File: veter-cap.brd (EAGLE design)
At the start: 101.6 x 78.7 mm, 36 parts, among them IC1 7805TV

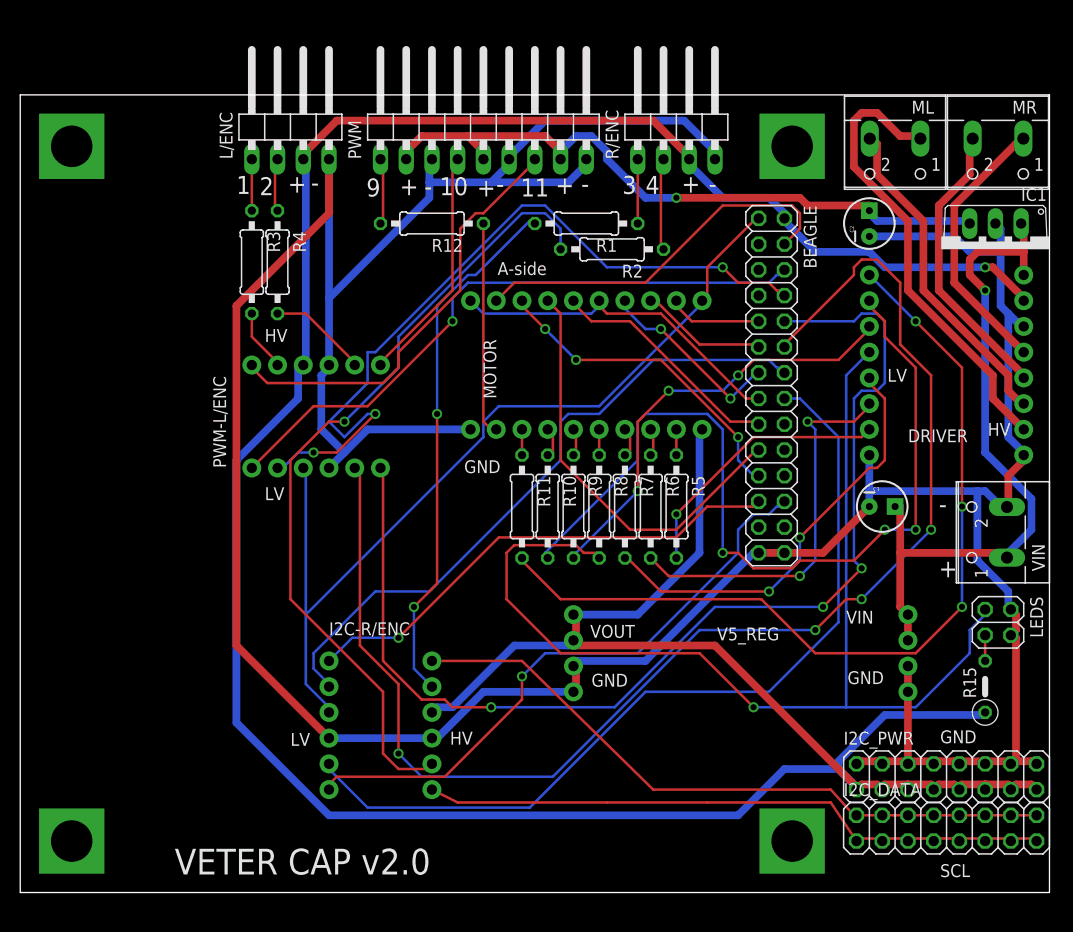
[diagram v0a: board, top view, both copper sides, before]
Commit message: version 3.0 of the cap, fixed connector
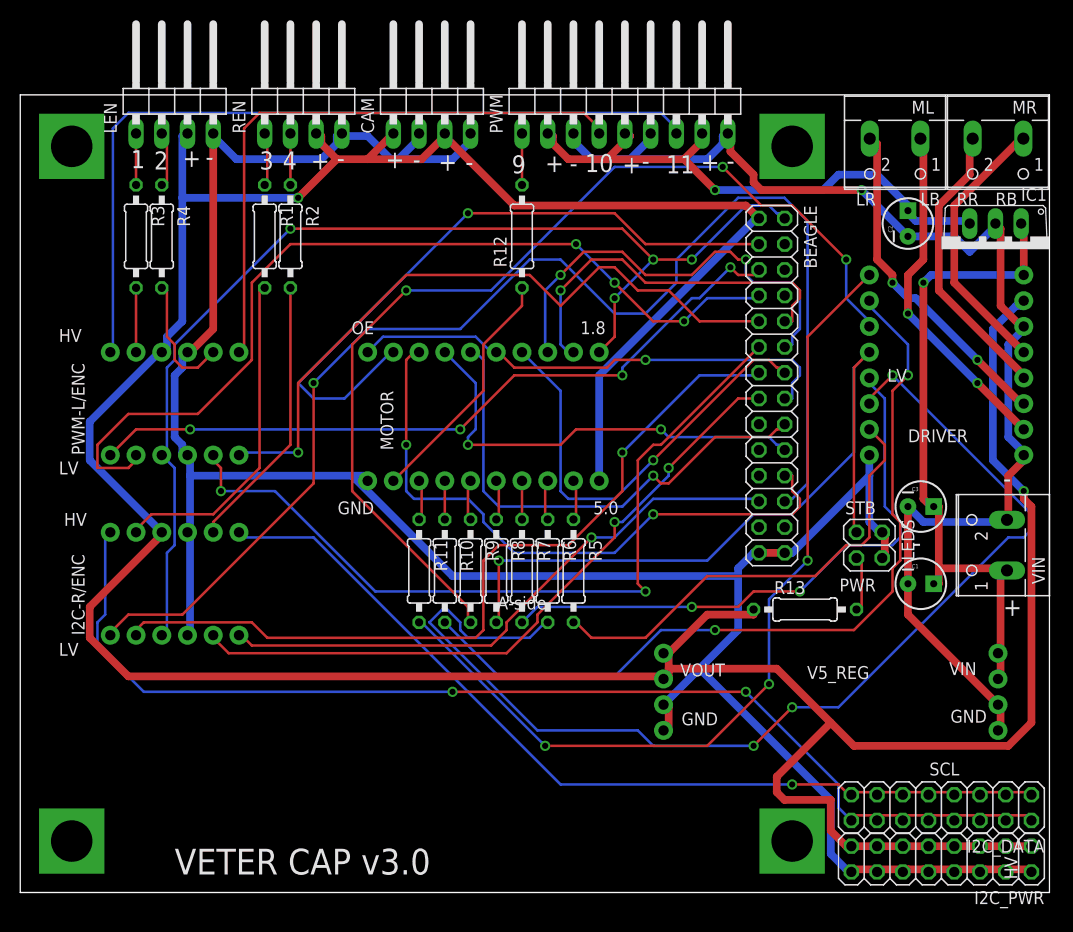
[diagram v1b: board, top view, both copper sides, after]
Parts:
- removed L/ENC: LEFT, pinhead:1X04/90
- removed R/ENC: RIGHT, pinhead:1X04/90
- removed R15: 560, resistor:0207/5V
- added C3: 10uF, SparkFun-Passives:CPOL-RADIAL-10UF-25V
- added CAM: PWR, pinhead:1X04/90
- added LEN: LEFT, pinhead:1X04/90
- added R13: 560, resistor:0207/10
- added REN: RIGHT, pinhead:1X04/90
- BEAGLE: value Expansion -> EXPANSION; device pinhead:2X14 -> veter:BEAGLE_PINH2X14
- moved R1 31.8 mm to (24.1, 64.8), turned to 270 degrees
- moved R2 31.8 mm to (26.7, 64.8), turned to 270 degrees
- moved I2C-R/ENC 24.7 mm to (15.2, 30.5), turned to 90 degrees
- moved LEDS 14.8 mm to (83.8, 34.3)
- moved PWM 14.2 mm to (59.7, 78.7)
- moved PWM-L/ENC 14.0 mm to (15.2, 48.3)
- moved R10 12.0 mm to (41.9, 31.8)
- moved R11 12.0 mm to (39.4, 31.8)
- moved R5 12.0 mm to (54.6, 31.8)
- moved R6 12.0 mm to (52.1, 31.8)
- moved R7 12.0 mm to (49.5, 31.8)
- moved R8 12.0 mm to (47.0, 31.8)
- moved R9 12.0 mm to (44.5, 31.8)
- moved R3 11.7 mm to (11.4, 64.8)
- moved R4 11.7 mm to (14.0, 64.8)
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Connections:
- removed net GND: BEAGLE.27, BEAGLE.28, C1.2, C2.2, DRIVER.1, DRIVER.11, DRIVER.16, I2C-R/ENC.10, I2C-R/ENC.3, I2C_PWR.10, I2C_PWR.12, I2C_PWR.14, I2C_PWR.16, I2C_PWR.2, I2C_PWR.4, I2C_PWR.6, I2C_PWR.8, IC1.2, L/ENC.4, LEDS.2, LEDS.4, MOTOR.20, PWM-L/ENC.10, PWM-L/ENC.3, PWM.3, PWM.6, PWM.9, R/ENC.4, V5_REG.3, V5_REG.4, V5_REG.5, V5_REG.6, VIN.2
- new net OE: BEAGLE.27, BEAGLE.28, CAM.2, CAM.4, DRIVER.1, I2C-R/ENC.10, I2C-R/ENC.3, I2C_PWR.10, I2C_PWR.12, I2C_PWR.14, I2C_PWR.16, I2C_PWR.2, I2C_PWR.4, I2C_PWR.6, I2C_PWR.8, LEDS.2, LEDS.4, LEN.4, MOTOR.20, PWM-L/ENC.10, PWM-L/ENC.3, REN.4, V5_REG.5, V5_REG.6
- new net PE: C1.2, C2.2, C3.2, DRIVER.11, DRIVER.16, IC1.2, PWM.3, PWM.6, PWM.9, V5_REG.3, V5_REG.4, VIN.2
- net +5V: now also CAM.1, CAM.3, LEN.3, R13.1, REN.3; no longer L/ENC.3, R/ENC.3, R15.1
- net N$12: now also REN.1; no longer R/ENC.1
- net N$13: now also REN.2; no longer R/ENC.2
- net N$14: now also LEN.1; no longer L/ENC.1
- net N$15: now also LEN.2; no longer L/ENC.2
- net N$24: now also R13.2; no longer R15.2
- net VBAT: now also C3.1
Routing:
- net GND: track 364.6 -> 0.00 mm
- net OE: track 0.00 -> 243.6 mm
- net PE: track 0.00 -> 125.0 mm, vias 0 -> 1
- net GPIO_183: track 48.9 -> 128.2 mm
- net N$18: track 38.6 -> 112.6 mm, vias 2 -> 3
- net N$21: track 42.9 -> 99.8 mm
- net GPIO_158: track 136.1 -> 79.7 mm, vias 4 -> 2
- net ENC4_161: track 79.7 -> 27.3 mm, vias 1 -> 0
- net I2C_SDA: track 66.0 -> 117.3 mm, vias 0 -> 2
- net GPIO_145: track 111.5 -> 67.7 mm, vias 3 -> 1
- net PWM11: track 42.9 -> 79.7 mm
- net PWM10: track 23.7 -> 59.4 mm
- net N$20: track 108.2 -> 74.9 mm
- net GPIO_135: track 12.7 -> 43.9 mm, vias 0 -> 2
- net GPIO_130: track 32.2 -> 62.4 mm, vias 3 -> 2
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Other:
- board text added: "1.8"
- board text added: "5.0"
- board text added: "LB"
- board text added: "LR"
- board text added: "OE"
- board text added: "PWR"
- board text added: "RB"
- board text added: "RR"
- board text added: "STB"
- board text added: "VETER CAP v3.0"
- board text removed: "VETER CAP v2.0"
